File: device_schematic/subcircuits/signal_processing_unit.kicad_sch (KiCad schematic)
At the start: 30 parts

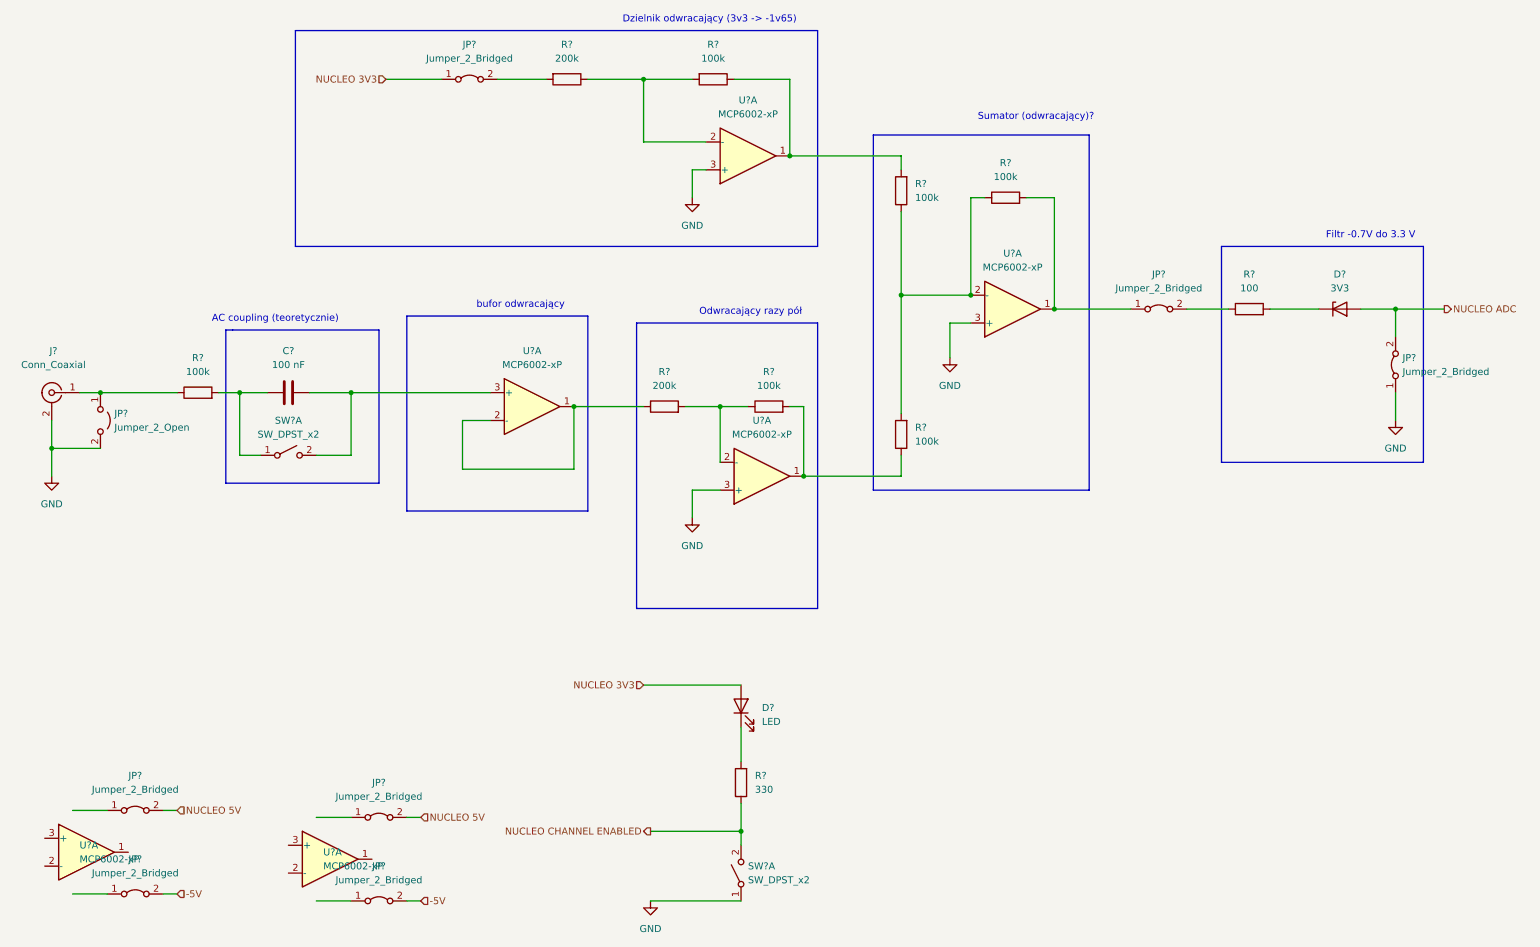
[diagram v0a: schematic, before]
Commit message: Device schematic finished version
+ correction to use D7 in place of D13
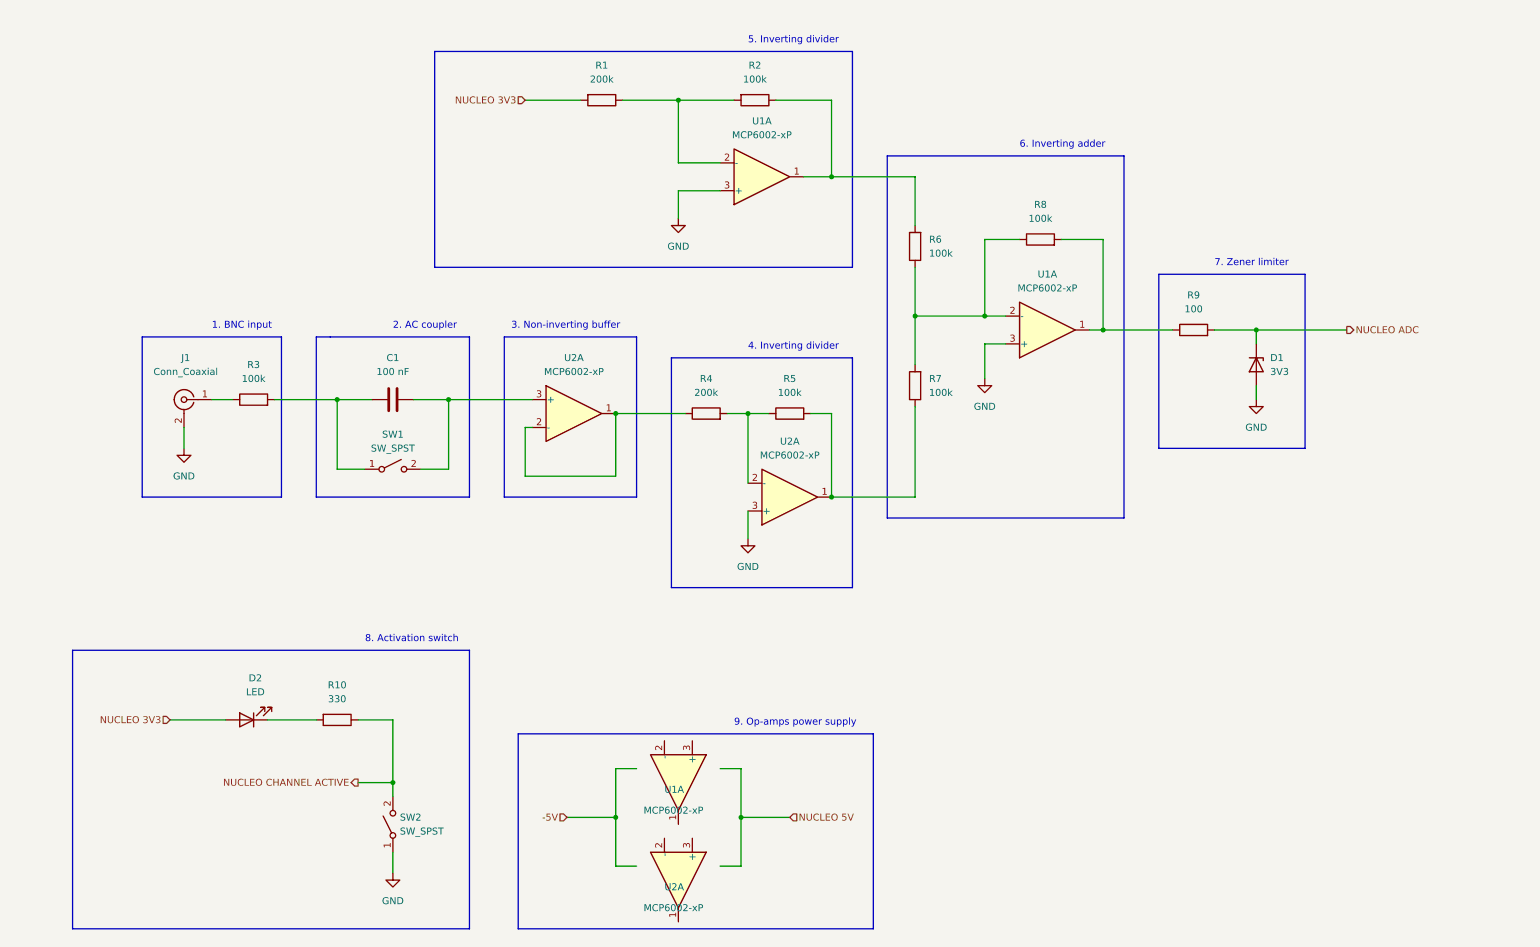
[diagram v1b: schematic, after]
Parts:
- removed JP? (x7): Jumper_2_Bridged, symbol Jumper:Jumper_2_Bridged
- removed JP?: Jumper_2_Open, symbol Jumper:Jumper_2_Open
- removed SW? (x2): SW_DPST_x2, symbol Switch:SW_DPST_x2
- removed U? (x6): MCP6002-xP, symbol Amplifier_Operational:MCP6002-xP
- added SW1, SW2: SW_SPST, symbol Switch:SW_SPST
- added U1 (x3), U2 (x3): MCP6002-xP, symbol Amplifier_Operational:MCP6002-xP
- gave numbers to parts that had none: 14
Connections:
- net GND: now also D1.2 (A), SW2.1 (A), U1.3 (+), U1.3 (+), U2.3 (+)
- net NUCLEO 3V3: now also R1.2
- net NUCLEO ADC: now also D1.1 (K), R9.2; no longer D1.2 (A)
- net at C1.1, R3.2: now also SW1.1 (A)
- net at C1.2: now also SW1.2 (B), U2.3 (+)
- net at R1.1, R2.2: now also U1.2 (-)
- net at R5.2, R7.1: now also U2.1
- net at R4.2, R5.1: now also U2.2 (-)
- net at R6.1, R7.2, R8.1: now also U1.2 (-)
- net at R2.1, R6.2: now also U1.1
- net at R8.2: now also R9.1, U1.1
- net at R4.1: now also U2.1, U2.2 (-)
- net NUCLEO CHANNEL ENABLED renamed NUCLEO CHANNEL ACTIVE
- net NUCLEO CHANNEL ACTIVE: now also SW2.2 (B)
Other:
- note added: "1. BNC input"
- note added: "2. AC coupler"
- note added: "3. Non-inverting buffer"
- note added: "4. Inverting divider"
- note added: "5. Inverting divider"
- note added: "6. Inverting adder"
- note added: "7. Zener limiter"
- note added: "8. Activation switch"
- note added: "9. Op-amps power supply"
- note removed: "AC coupling (teoretycznie)"
- note removed: "Dzielnik odwracający (3v3 -> -1v65)"
- note removed: "Filtr -0.7V do 3.3 V"
- note removed: "Odwracający razy pół"
- note removed: "Sumator (odwracający)?"
- note removed: "bufor odwracający"
- moved on the sheet: C1, D1, D2, J1, R1, R10, R2, R3, R4, R5, R6, R7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
